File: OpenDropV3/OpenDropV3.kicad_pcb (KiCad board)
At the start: 2 copper layers, 100 x 112 mm, 270 parts, among them J1 USB_C_Receptacle, J2 Conn_02x05_Odd_Even, P1 CONN_01X01, P10 CONN_01X01, P11 CONN_01X01, P12 CONN_01X01, P13 ScrewPad1, P14 ScrewPad2, P15 ScrewPad3, P16 ScrewPad4, P2 ScrewPad4, P3 CONN_01X01, P4 CONN_PSEUDO_AC, P7 CONN_01X01, P8 CONN_01X01, P9 CONN_01X01, SW1 SW_PUSH, SW2 SW_PUSH, SW3 SW_PUSH, SW5 SPST, T1 TK560P60Y, U1 MAX1771ESA, U10 AQY210EH, U11 AQY210EH, U12 AQY210EH, U13 AQY210EH, U14 TLV1117-33, U15 MCP41010, U16 74xx14, U2 HV507, U3 PAM8301, U4 HV507, U5 SAMD21G18B-A changed from SAM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, U6 MCP6002, U7 HCPL0534, U8 HCPL0534, U9 HCPL0534, Y1 32.765

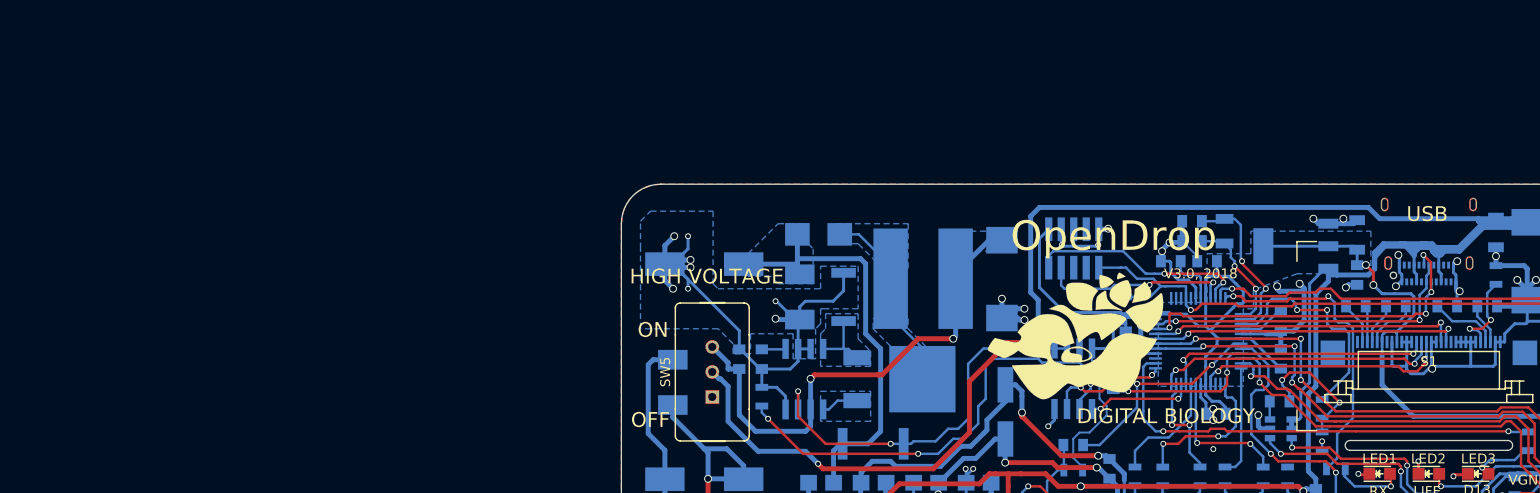
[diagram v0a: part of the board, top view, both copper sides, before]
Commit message: Adjusting PCB for more room around some components
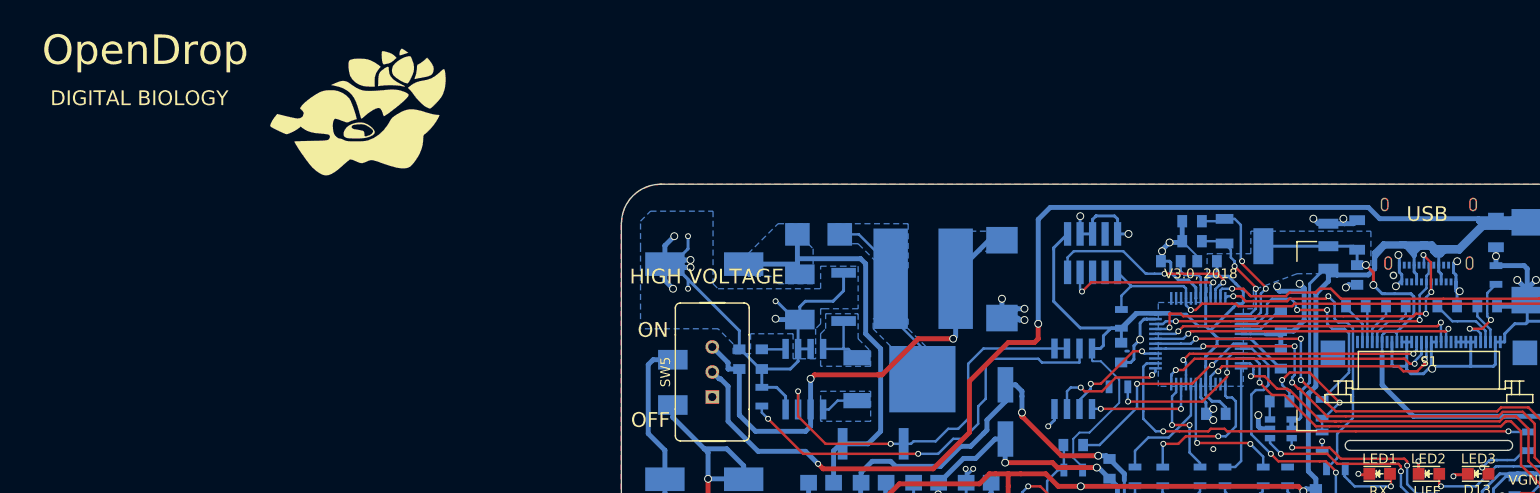
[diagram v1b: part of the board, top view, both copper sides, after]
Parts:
- moved G*** 76.3 mm to (23.4, 23.7)
- moved J2 1.97 mm to (97.8, 38.0)
- moved R5 1.36 mm to (100.8, 44.7)
- moved C14 1.24 mm to (100.8, 48.1)
- moved R9 0.77 mm to (100.5, 51.6), turned to 180 degrees
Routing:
- net Net-(R1-Pad1): track 47.0 -> 43.2 mm
- net RESET: track 60.0 -> 56.8 mm
- net +3V3: track 308.1 -> 304.8 mm
- net SWCLK: track 19.6 -> 17.5 mm
- net GND: track 363.8 -> 365.8 mm, vias 49 -> 48
- net SWDIO: track 22.8 -> 21.1 mm
- net V_USB: track 302.4 -> 301.1 mm
- net V_CS: track 10.8 -> 11.6 mm
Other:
- net class Default: trace_width 0.15 -> 0.25
